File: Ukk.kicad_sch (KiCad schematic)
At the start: 0 parts

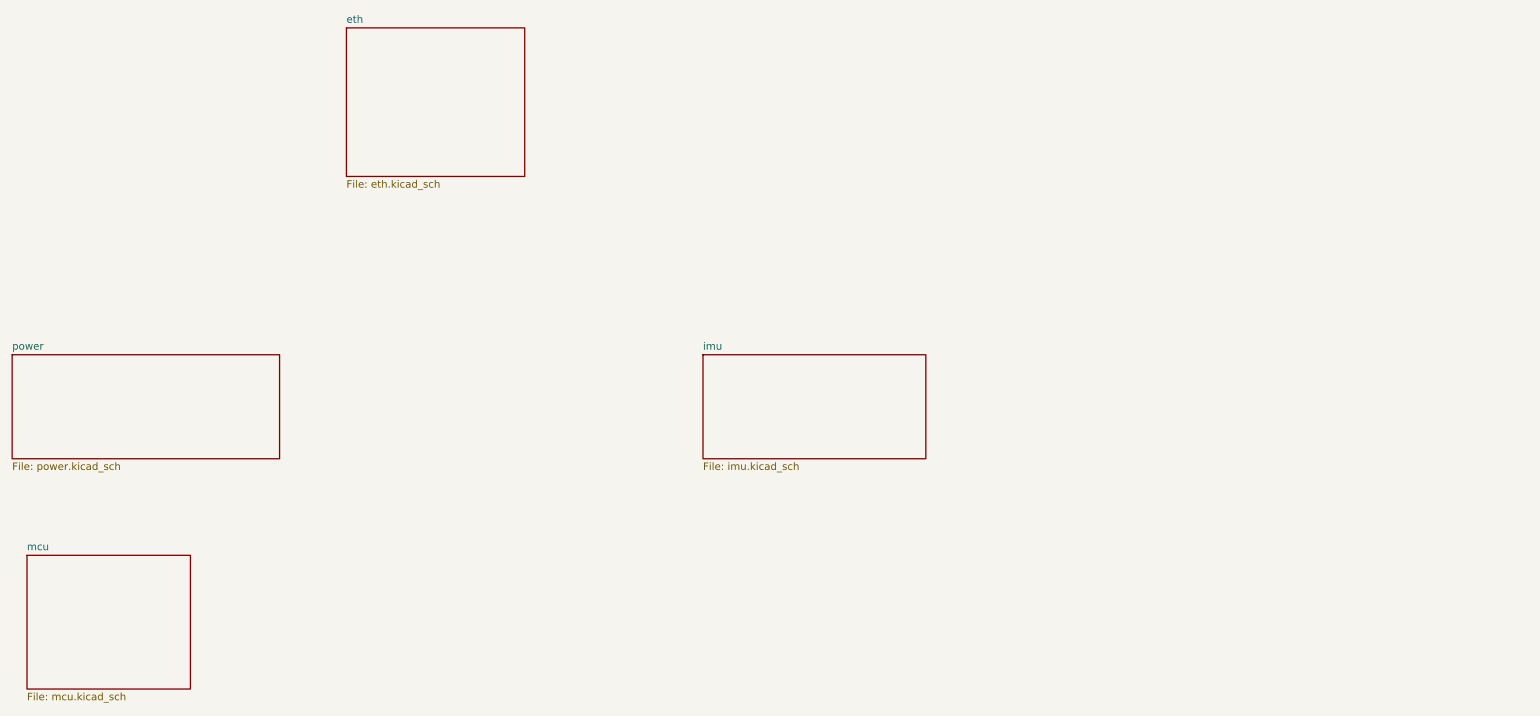
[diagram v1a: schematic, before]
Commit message: Usb Sd arayüzleri eklendi.
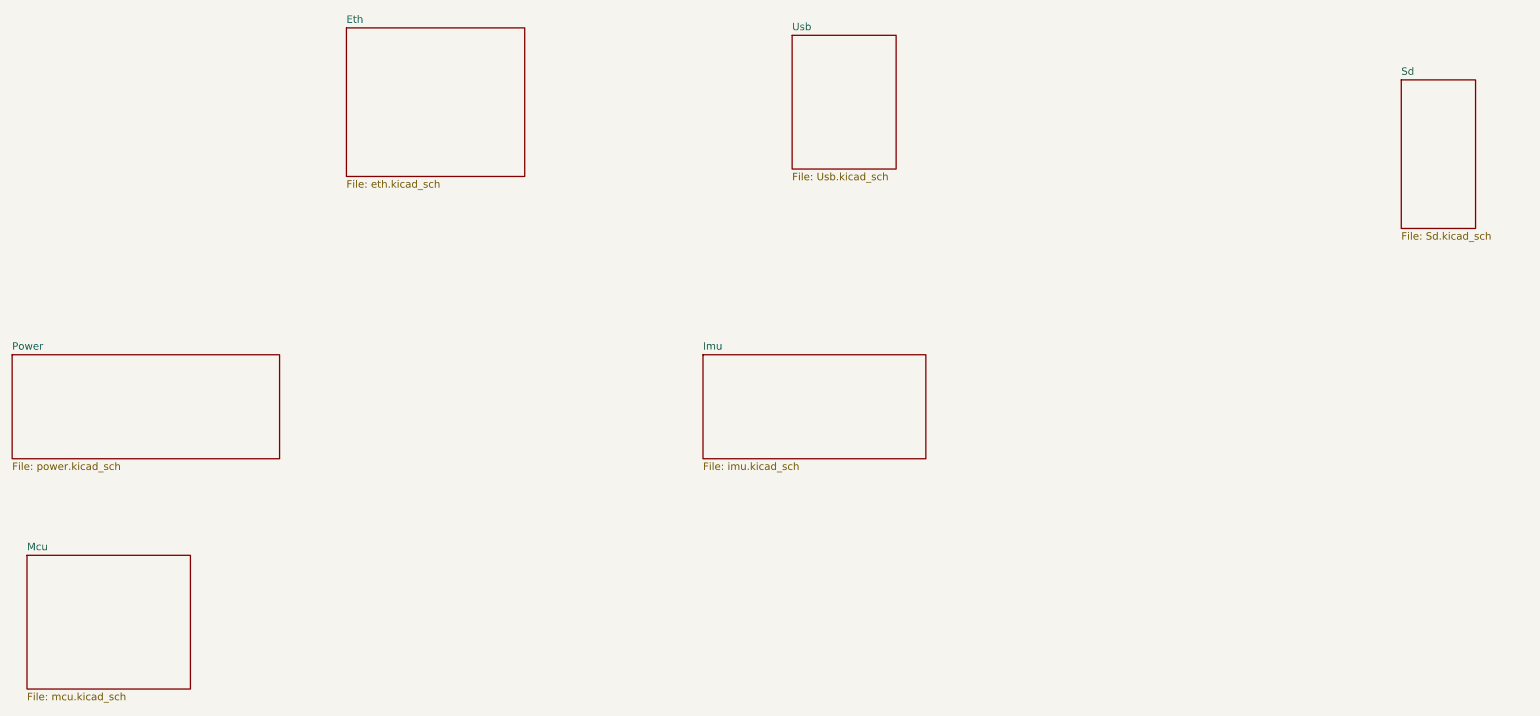
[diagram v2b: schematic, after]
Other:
- sheet eth renamed Eth
- sheet imu renamed Imu
- sheet mcu renamed Mcu
- sheet power renamed Power
- added sheet Sd (Sd.kicad_sch)
- added sheet Usb (Usb.kicad_sch)
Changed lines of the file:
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@@
 			(color 0 0 0 0)
 		)
-		(property "Sheetname" "power"
+		(property "Sheetname" "Power"
 			(at 36.83 114.8584 0)
 			(show_name no)
@@
 			(color 0 0 0 0)
 		)
-		(property "Sheetname" "imu"
+		(property "Sheetname" "Imu"
 			(at 154.94 114.8584 0)
 			(show_name no)
@@
 	)
 	(sheet
+		(at 170.18 60.96)
+		(size 17.78 22.86)
+		(exclude_from_sim no)
+		(in_bom yes)
+		(on_board yes)
+		(dnp no)
+		(fields_autoplaced yes)
+		(stroke
+			(width 0.1524)
+			(type solid)
+		)
+		(fill
+			(color 0 0 0 0)
+		)
+		(property "Sheetname" "Usb"
+			(at 170.18 60.2484 0)
+			(show_name no)
+			(do_not_autoplace no)
+			(effects
+				(font
+					(size 1.27 1.27)
+				)
+				(justify left bottom)
+			)
+		)
+		(property "Sheetfile" "Usb.kicad_sch"
+			(at 170.18 84.4046 0)
+			(show_name no)
+			(do_not_autoplace no)
+			(effects
+				(font
+					(size 1.27 1.27)
+				)
+				(justify left top)
+			)
+		)
+		(instances
+			(project "Ukk"
+				(path "/2375ab6f-0d27-47c2-8e53-820af89ba359"
+					(page "6")
+				)
+			)
+		)
+	)
+	(sheet
+		(at 274.32 68.58)
+		(size 12.7 25.4)
+		(exclude_from_sim no)
+		(in_bom yes)
+		(on_board yes)
+		(dnp no)
+		(fields_autoplaced yes)
+		(stroke
+			(width 0.1524)
+			(type solid)
+		)
+		(fill
+			(color 0 0 0 0)
+		)
+		(property "Sheetname" "Sd"
+			(at 274.32 67.8684 0)
+			(show_name no)
+			(do_not_autoplace no)
+			(effects
+				(font
+					(size 1.27 1.27)
+				)
+				(justify left bottom)
+			)
+		)
+		(property "Sheetfile" "Sd.kicad_sch"
+			(at 274.32 94.5646 0)
+			(show_name no)
+			(do_not_autoplace no)
+			(effects
+				(font
+					(size 1.27 1.27)
+				)
+				(justify left top)
+			)
+		)
+		(instances
+			(project "Ukk"
+				(path "/2375ab6f-0d27-47c2-8e53-820af89ba359"
+					(page "7")
+				)
+			)
+		)
+	)
+	(sheet
 		(at 93.98 59.69)
 		(size 30.48 25.4)
@@
 			(color 0 0 0 0)
 		)
-		(property "Sheetname" "eth"
+		(property "Sheetname" "Eth"
 			(at 93.98 58.9784 0)
 			(show_name no)
@@
 			(color 0 0 0 0)
 		)
-		(property "Sheetname" "mcu"
+		(property "Sheetname" "Mcu"
 			(at 39.37 149.1484 0)
 			(show_name no)

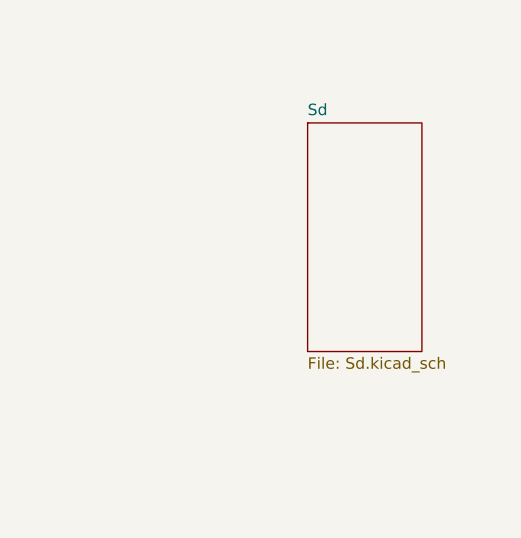
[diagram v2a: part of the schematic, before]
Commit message: Eth güncellendi.
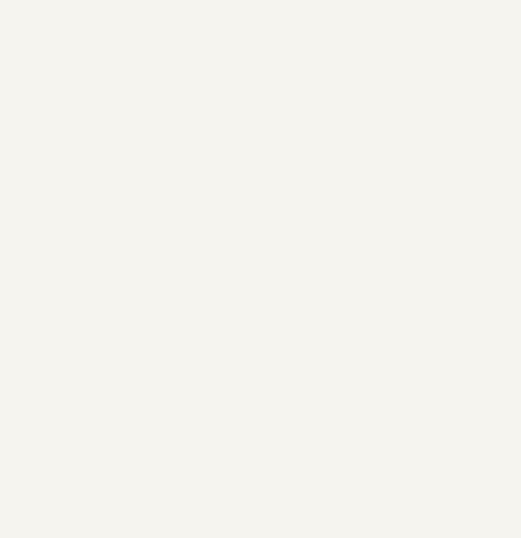
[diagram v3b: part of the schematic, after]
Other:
- removed sheet Sd
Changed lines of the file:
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@@
-	)
-	(sheet
-		(at 274.32 68.58)
-		(size 12.7 25.4)
-		(exclude_from_sim no)
-		(in_bom yes)
-		(on_board yes)
-		(dnp no)
-		(fields_autoplaced yes)
-		(stroke
-			(width 0.1524)
-			(type solid)
-		)
-		(fill
-			(color 0 0 0 0)
-		)
-		(property "Sheetname" "Sd"
-			(at 274.32 67.8684 0)
-			(show_name no)
-			(do_not_autoplace no)
-			(effects
-				(font
-					(size 1.27 1.27)
-				)
-				(justify left bottom)
-			)
-		)
-		(property "Sheetfile" "Sd.kicad_sch"
-			(at 274.32 94.5646 0)
-			(show_name no)
-			(do_not_autoplace no)
-			(effects
-				(font
-					(size 1.27 1.27)
-				)
-				(justify left top)
-			)
-		)
-		(instances
-			(project "Ukk"
-				(path "/2375ab6f-0d27-47c2-8e53-820af89ba359"
-					(page "7")
-				)
-			)
-		)
 	)
 	(sheet

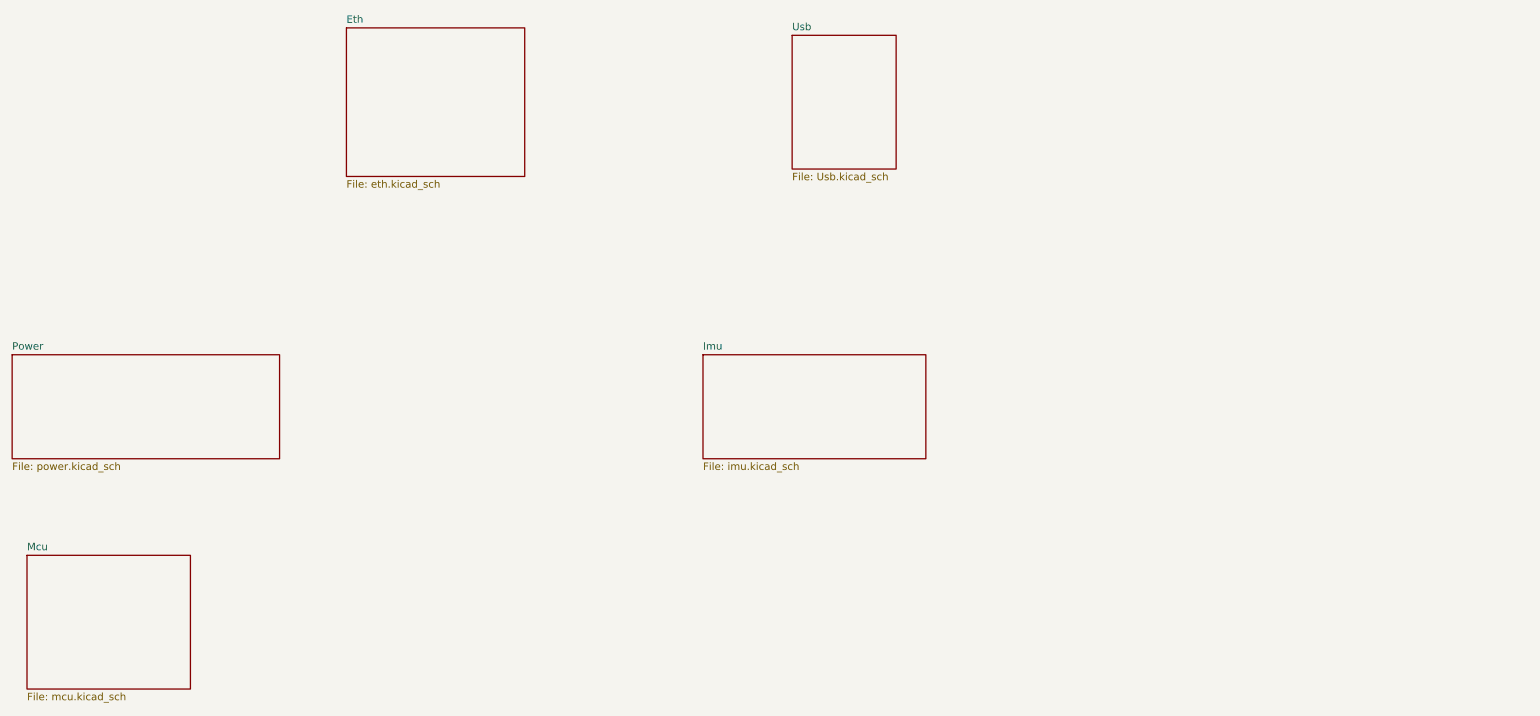
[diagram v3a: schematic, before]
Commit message: Sdram ve power kaldırıldı.
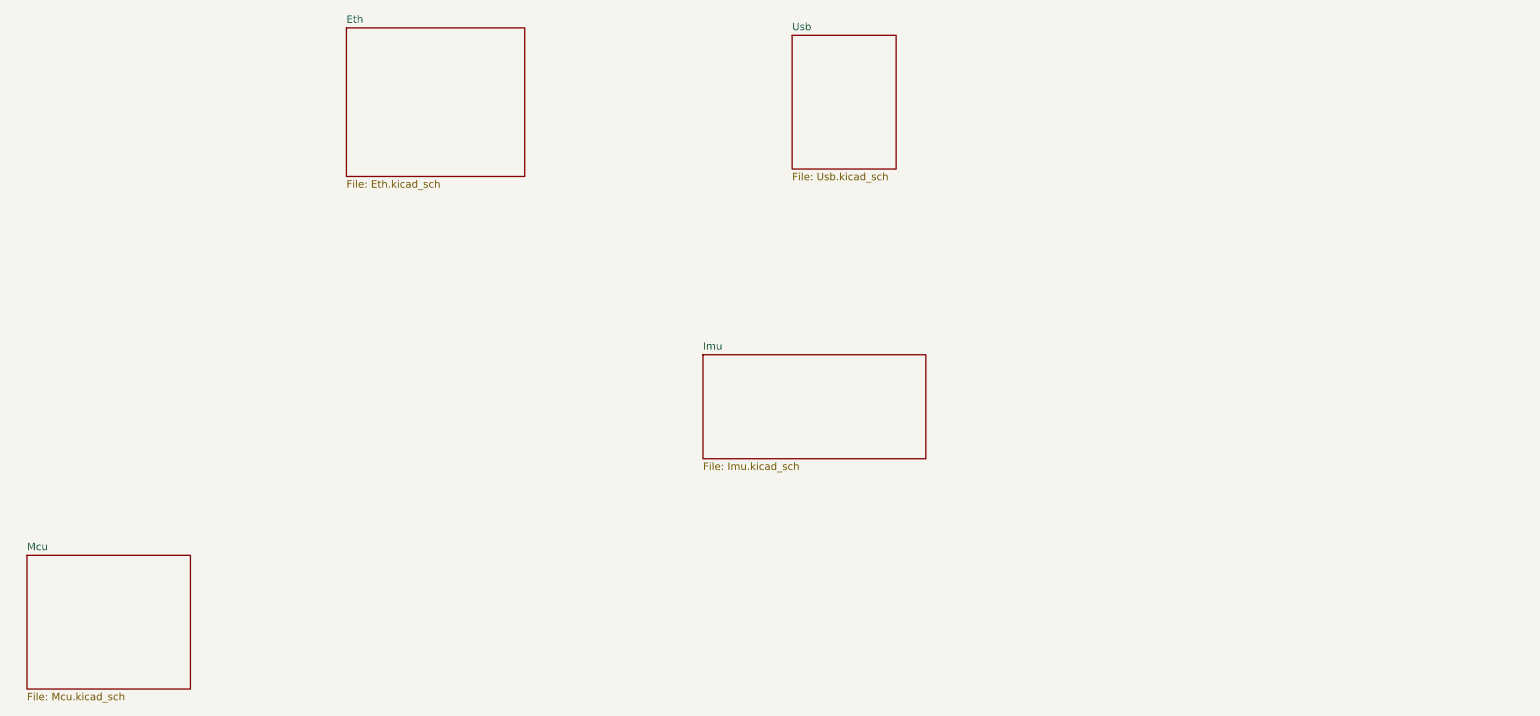
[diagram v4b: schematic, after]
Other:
- removed sheet Power
- sheet Eth: file eth.kicad_sch -> Eth.kicad_sch
- sheet Imu: file imu.kicad_sch -> Imu.kicad_sch
- sheet Mcu: file mcu.kicad_sch -> Mcu.kicad_sch
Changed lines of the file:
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@@
 	(paper "A4")
-	(sheet
-		(at 36.83 115.57)
-		(size 45.72 17.78)
-		(exclude_from_sim no)
-		(in_bom yes)
-		(on_board yes)
-		(dnp no)
-		(fields_autoplaced yes)
-		(stroke
-			(width 0.1524)
-			(type solid)
-		)
-		(fill
-			(color 0 0 0 0)
-		)
-		(property "Sheetname" "Power"
-			(at 36.83 114.8584 0)
-			(show_name no)
-			(do_not_autoplace no)
-			(effects
-				(font
-					(size 1.27 1.27)
-				)
-				(justify left bottom)
-			)
-		)
-		(property "Sheetfile" "power.kicad_sch"
-			(at 36.83 133.9346 0)
-			(show_name no)
-			(do_not_autoplace no)
-			(effects
-				(font
-					(size 1.27 1.27)
-				)
-				(justify left top)
-			)
-		)
-		(instances
-			(project "Ukk"
-				(path "/2375ab6f-0d27-47c2-8e53-820af89ba359"
-					(page "4")
-				)
-			)
-		)
-	)
 	(sheet
 		(at 154.94 115.57)
@@
 			)
 		)
-		(property "Sheetfile" "imu.kicad_sch"
+		(property "Sheetfile" "Imu.kicad_sch"
 			(at 154.94 133.9346 0)
 			(show_name no)
@@
 			)
 		)
-		(property "Sheetfile" "eth.kicad_sch"
+		(property "Sheetfile" "Eth.kicad_sch"
 			(at 93.98 85.6746 0)
 			(show_name no)
@@
 			)
 		)
-		(property "Sheetfile" "mcu.kicad_sch"
+		(property "Sheetfile" "Mcu.kicad_sch"
 			(at 39.37 173.3046 0)
 			(show_name no)
